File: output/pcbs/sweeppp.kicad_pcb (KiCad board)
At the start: 2 copper layers, 136.5 x 111 mm, 61 parts

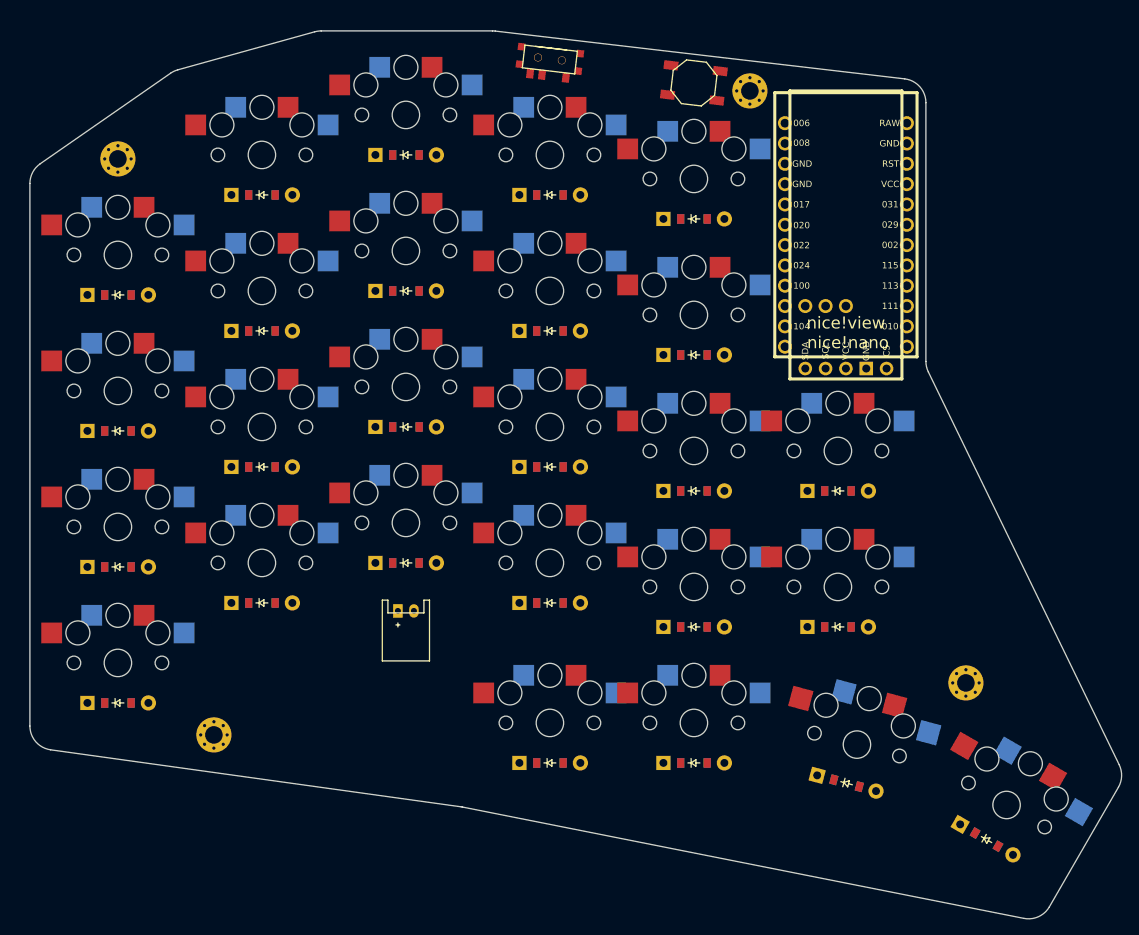
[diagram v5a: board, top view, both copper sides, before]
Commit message: Adjusted inner2 column to align with screen
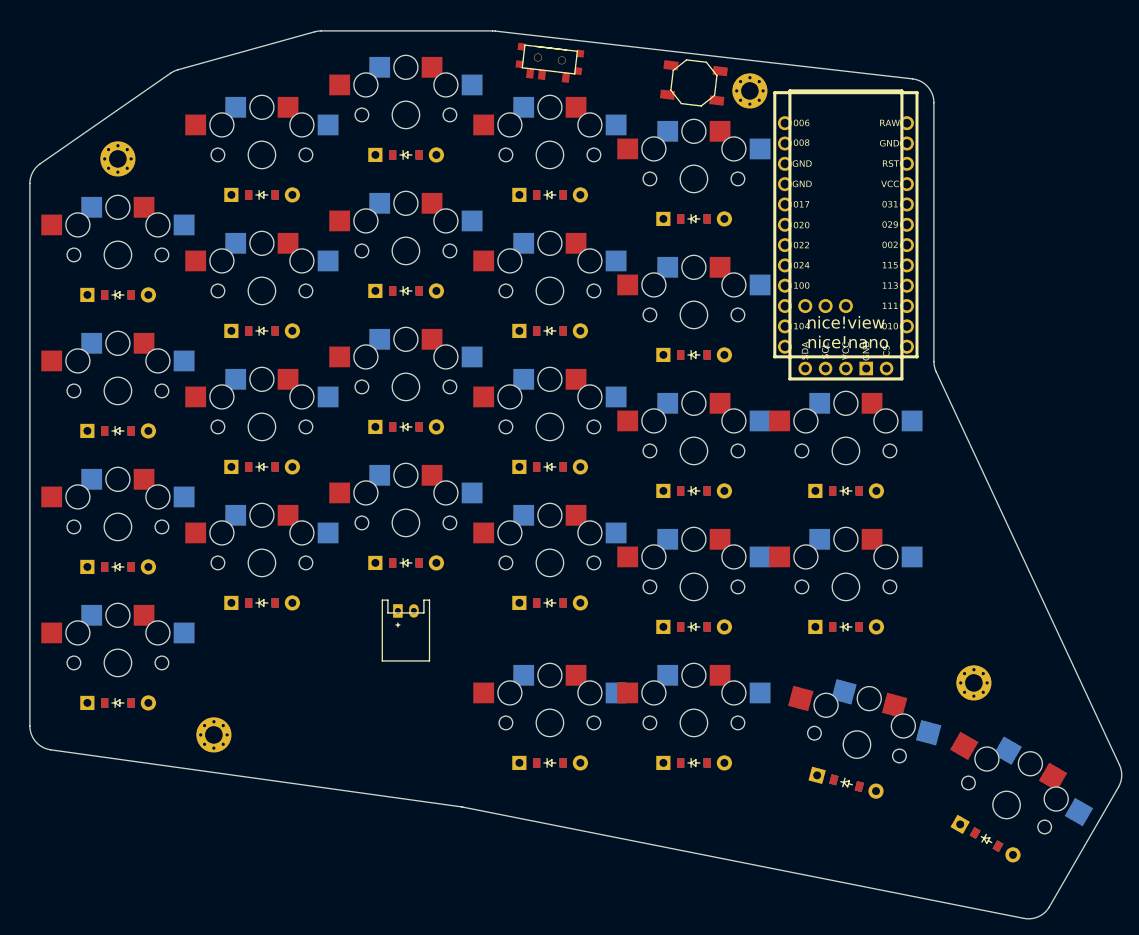
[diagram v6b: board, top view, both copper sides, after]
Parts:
- moved D21 1.00 mm to (191.0, 95.5)
- moved D22 1.00 mm to (191.0, 78.5)
- moved S21 1.00 mm to (191.0, 90.5)
- moved S22 1.00 mm to (191.0, 73.5)
- moved _4 1.00 mm to (207.0, 102.5)
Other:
- outline, holes or cut-outs redrawn
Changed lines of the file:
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@@
         )
       (module PG1350 (layer F.Cu)
-      (at 190 90.5 0)
+      (at 191 90.5 0)
       (fp_text reference "S21" (at 0 0) (layer F.SilkS) hide (effects (font (size 1.27 1.27) (thickness 0.15))))
       (fp_text value "" (at 0 0) (layer F.SilkS) hide (effects (font (size 1.27 1.27) (thickness 0.15))))
@@
         )
       (module PG1350 (layer F.Cu)
-      (at 190 73.5 0)
+      (at 191 73.5 0)
       (fp_text reference "S22" (at 0 0) (layer F.SilkS) hide (effects (font (size 1.27 1.27) (thickness 0.15))))
       (fp_text value "" (at 0 0) (layer F.SilkS) hide (effects (font (size 1.27 1.27) (thickness 0.15))))
@@
     )
     (module ComboDiode (layer F.Cu)
-        (at 190 95.5 0)
+        (at 191 95.5 0)
         (fp_text reference "D21" (at 0 0) (layer F.SilkS) hide (effects (font (size 1.27 1.27) (thickness 0.15))))
         (fp_text value "" (at 0 0) (layer F.SilkS) hide (effects (font (size 1.27 1.27) (thickness 0.15))))
@@
     )
     (module ComboDiode (layer F.Cu)
-        (at 190 78.5 0)
+        (at 191 78.5 0)
         (fp_text reference "D22" (at 0 0) (layer F.SilkS) hide (effects (font (size 1.27 1.27) (thickness 0.15))))
         (fp_text value "" (at 0 0) (layer F.SilkS) hide (effects (font (size 1.27 1.27) (thickness 0.15))))
@@
     )
     (module "MountingHole_2.2mm_M2_Pad_Via" (version 20210722) (generator pcbnew) (layer "F.Cu")
-      (at 206 102.5 0)
+      (at 207 102.5 0)
       (fp_text reference "_4" (at 0 -3.2) (layer "F.SilkS") hide
         (effects (font (size 1 1) (thickness 0.15)))
@@
 (gr_line (start 90.28881264685059 37.60499121746486) (end 106.58203879351727 26.29025083783523) (angle 90) (layer Edge.Cuts) (width 0.15))
 (gr_line (start 107.49029445382999 25.863807096158343) (end 124.60599322716334 21.109446325787964) (angle 90) (layer Edge.Cuts) (width 0.15))
-(gr_line (start 125.40892492 21) (end 146.8255916142857 21) (angle 90) (layer Edge.Cuts) (width 0.15))
-(gr_line (start 147.1732337257957 21.020210601342832) (end 198.34764211150997 26.990558246342825) (angle 90) (layer Edge.Cuts) (width 0.15))
-(gr_line (start 201 29.970347644999997) (end 201 62.30976752331668) (angle 90) (layer Edge.Cuts) (width 0.15))
-(gr_line (start 201.3016461 63.62083052331667) (end 225.1632542897898 112.73140977378557) (angle 90) (layer Edge.Cuts) (width 0.15))
-(gr_line (start 225.06297658978986 115.54247277378556) (end 216.43333215961238 130.48945531278997) (angle 90) (layer Edge.Cuts) (width 0.15))
+(gr_line (start 125.40892492 21) (end 146.82874165555558 21) (angle 90) (layer Edge.Cuts) (width 0.15))
+(gr_line (start 147.17014556686178 21.01948940129508) (end 199.34140391130617 26.995469902567795) (angle 90) (layer Edge.Cuts) (width 0.15))
+(gr_line (start 202 29.97598050127272) (end 202 62.334887266599594) (angle 90) (layer Edge.Cuts) (width 0.15))
+(gr_line (start 202.28109995616538 63.60279198704097) (end 225.19905252479415 112.74815065663205) (angle 90) (layer Edge.Cuts) (width 0.15))
+(gr_line (start 225.07822868095957 115.51605537707337) (end 216.43333215961243 130.48945531278986) (angle 90) (layer Edge.Cuts) (width 0.15))
 (gr_line (start 213.25166863674693 131.932145528087) (end 143.08502521190636 118.01686199984744) (angle 90) (layer Edge.Cuts) (width 0.15))
 (gr_line (start 142.91414307352233 117.9880754268781) (end 91.58729481551853 110.85934650215535) (angle 90) (layer Edge.Cuts) (width 0.15))
@@
 (gr_arc (start 108.29322614666665 28.75436077037037) (end 107.49029444666665 25.86380707037037) (angle -19.253716654027485) (layer Edge.Cuts) (width 0.15))
 (gr_arc (start 125.40892492 24) (end 125.40892492 21) (angle -15.524113143634992) (layer Edge.Cuts) (width 0.15))
-(gr_arc (start 146.8255916142857 24) (end 147.17323371428571 21.0202106) (angle -6.654425330555455) (layer Edge.Cuts) (width 0.15))
-(gr_arc (start 198 29.970347644999997) (end 201 29.970347644999997) (angle -83.34557466944511) (layer Edge.Cuts) (width 0.15))
-(gr_arc (start 204 62.30976752331668) (end 201 62.30976752331668) (angle -25.913963195184778) (layer Edge.Cuts) (width 0.15))
-(gr_arc (start 222.4649003897898 114.04247277378556) (end 225.0629765897898 115.54247277378556) (angle -55.9139633036003) (layer Edge.Cuts) (width 0.15))
-(gr_arc (start 213.8352559596124 128.98945531278997) (end 213.2516686596124 131.93214551278996) (angle -71.21721666545687) (layer Edge.Cuts) (width 0.15))
+(gr_arc (start 146.82874165555558 24) (end 147.17014555555556 21.0194894) (angle -6.534490900977929) (layer Edge.Cuts) (width 0.15))
+(gr_arc (start 199 29.97598050127272) (end 202 29.97598050127272) (angle -83.46550909902264) (layer Edge.Cuts) (width 0.15))
+(gr_arc (start 205 62.334887266599594) (end 202 62.334887266599594) (angle -25.001052542281315) (layer Edge.Cuts) (width 0.15))
+(gr_arc (start 222.48015248095953 114.01605537707343) (end 225.07822868095954 115.51605537707343) (angle -55.001052650696224) (layer Edge.Cuts) (width 0.15))
+(gr_arc (start 213.83525595961243 128.98945531278991) (end 213.25166865961242 131.9321455127899) (angle -71.21721666545847) (layer Edge.Cuts) (width 0.15))
 (gr_arc (start 142.5014378890409 120.95955221514457) (end 143.0850251890409 118.01686201514457) (angle -3.310052652139106) (layer Edge.Cuts) (width 0.15))
 (gr_arc (start 92 107.88786971388888) (end 89 107.88786971388888) (angle -82.09283587826559) (layer Edge.Cuts) (width 0.15))

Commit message: Routed pcb
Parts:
- MCU1: value nice_nano -> (none); footprint nice_nano -> ceoloide:mcu_nice_nano
- moved MCU1 3.25 mm to (189.3, 43.7), turned to 0 degrees
- moved T1 2.44 mm to (152.3, 22.7)
- moved S25 2.44 mm to (190.7, 108.4)
- moved D13 2.44 mm to (152.3, 90.7)
- moved niceView1 2.44 mm to (189.3, 62.7)
- moved S11 2.44 mm to (134.3, 46.7)
- moved _2 2.44 mm to (110.3, 107.2)
- moved D19 2.44 mm to (170.3, 59.7)
- moved D8 2.44 mm to (116.3, 39.7)
- moved _1 2.44 mm to (98.3, 35.2)
- moved D3 2.44 mm to (98.3, 69.2)
- moved D6 2.44 mm to (116.3, 73.7)
- moved S18 2.44 mm to (170.3, 71.7)
- moved S2 2.44 mm to (98.3, 81.2)
- moved S9 2.44 mm to (134.3, 80.7)
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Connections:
- net P006 renamed MCU1_1
- net P008 renamed MCU1_2
- net P029 renamed MCU1_19
- net P031 renamed MCU1_20
- D1 pad 1: P022 -> P7
- D10 pad 1: P024 -> P8
- D11 pad 1: P100 -> P16
- D12 pad 1: P011 -> P21
- D13 pad 1: P022 -> P7
- D14 pad 1: P024 -> P8
- D15 pad 1: P100 -> P16
- D16 pad 1: P011 -> P21
- D17 pad 1: P022 -> P7
- D18 pad 1: P024 -> P8
- D19 pad 1: P100 -> P16
- D2 pad 1: P024 -> P8
- D20 pad 1: P011 -> P21
- D21 pad 1: P022 -> P7
- D22 pad 1: P024 -> P8
- D23 pad 1: P104 -> P6
- D24 pad 1: P104 -> P6
- D25 pad 1: P104 -> P6
- D26 pad 1: P104 -> P6
- D3 pad 1: P100 -> P16
- D4 pad 1: P011 -> P21
- D5 pad 1: P022 -> P7
- D6 pad 1: P024 -> P8
- D7 pad 1: P100 -> P16
- D8 pad 1: P011 -> P21
- D9 pad 1: P022 -> P7
- MCU1 pad 10: P011 -> MCU1_10
- MCU1 pad 11: P104 -> MCU1_11
- MCU1 pad 12: P106 -> MCU1_12
- MCU1 pad 13: P009 -> MCU1_13
- MCU1 pad 14: P010 -> MCU1_14
- MCU1 pad 15: P111 -> MCU1_15
- MCU1 pad 16: P113 -> MCU1_16
- MCU1 pad 17: P115 -> MCU1_17
- MCU1 pad 18: P002 -> MCU1_18
- MCU1 pad 21: VCC -> MCU1_21
- MCU1 pad 22: RST -> MCU1_22
- MCU1 pad 23: GND -> MCU1_23
- MCU1 pad 24: RAW -> MCU1_24
- MCU1 pad 3: GND -> MCU1_3
- MCU1 pad 4: GND -> MCU1_4
- MCU1 pad 5: P017 -> MCU1_5
- MCU1 pad 6: P020 -> MCU1_6
- MCU1 pad 7: P022 -> MCU1_7
- MCU1 pad 8: P024 -> MCU1_8
- MCU1 pad 9: P100 -> MCU1_9
- S1 pad 1: P115 -> P20
- S10 pad 1: P111 -> P18
- S11 pad 1: P111 -> P18
- S12 pad 1: P111 -> P18
- S13 pad 1: P010 -> P15
- S14 pad 1: P010 -> P15
- S15 pad 1: P010 -> P15
- S16 pad 1: P010 -> P15
- S17 pad 1: P009 -> P10
- S18 pad 1: P009 -> P10
- S19 pad 1: P009 -> P10
- S2 pad 1: P115 -> P20
- S20 pad 1: P009 -> P10
- S21 pad 1: P106 -> P9
- S22 pad 1: P106 -> P9
- S23 pad 1: P111 -> P18
- S24 pad 1: P010 -> P15
- S25 pad 1: P009 -> P10
- S26 pad 1: P106 -> P9
- S3 pad 1: P115 -> P20
- S4 pad 1: P115 -> P20
- S5 pad 1: P113 -> P19
- S6 pad 1: P113 -> P19
- S7 pad 1: P113 -> P19
- S8 pad 1: P113 -> P19
- S9 pad 1: P111 -> P18
- niceView1 pad 1: P002 -> P4
- niceView1 pad 4: P020 -> P3
- niceView1 pad 5: P017 -> P2
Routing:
- net P20: track 0.00 -> 201.3 mm, vias 0 -> 4
- net P18: track 0.00 -> 192.4 mm, vias 0 -> 6
- net GND: track 0.00 -> 192.0 mm, vias 0 -> 1
- net P7: track 0.00 -> 179.3 mm
- net P19: track 0.00 -> 175.2 mm, vias 0 -> 4
- net P15: track 0.00 -> 172.4 mm, vias 0 -> 5
- net P8: track 0.00 -> 165.3 mm
- net P10: track 0.00 -> 157.9 mm, vias 0 -> 5
- net P6: track 0.00 -> 148.9 mm
- net P21: track 0.00 -> 129.4 mm
- net P16: track 0.00 -> 128.2 mm
- net P9: track 0.00 -> 109.2 mm, vias 0 -> 3
- net BAT: track 0.00 -> 77.7 mm, vias 0 -> 1
- net VCC: track 0.00 -> 47.8 mm
- net RAW: track 0.00 -> 45.2 mm
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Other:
- net class Default removed

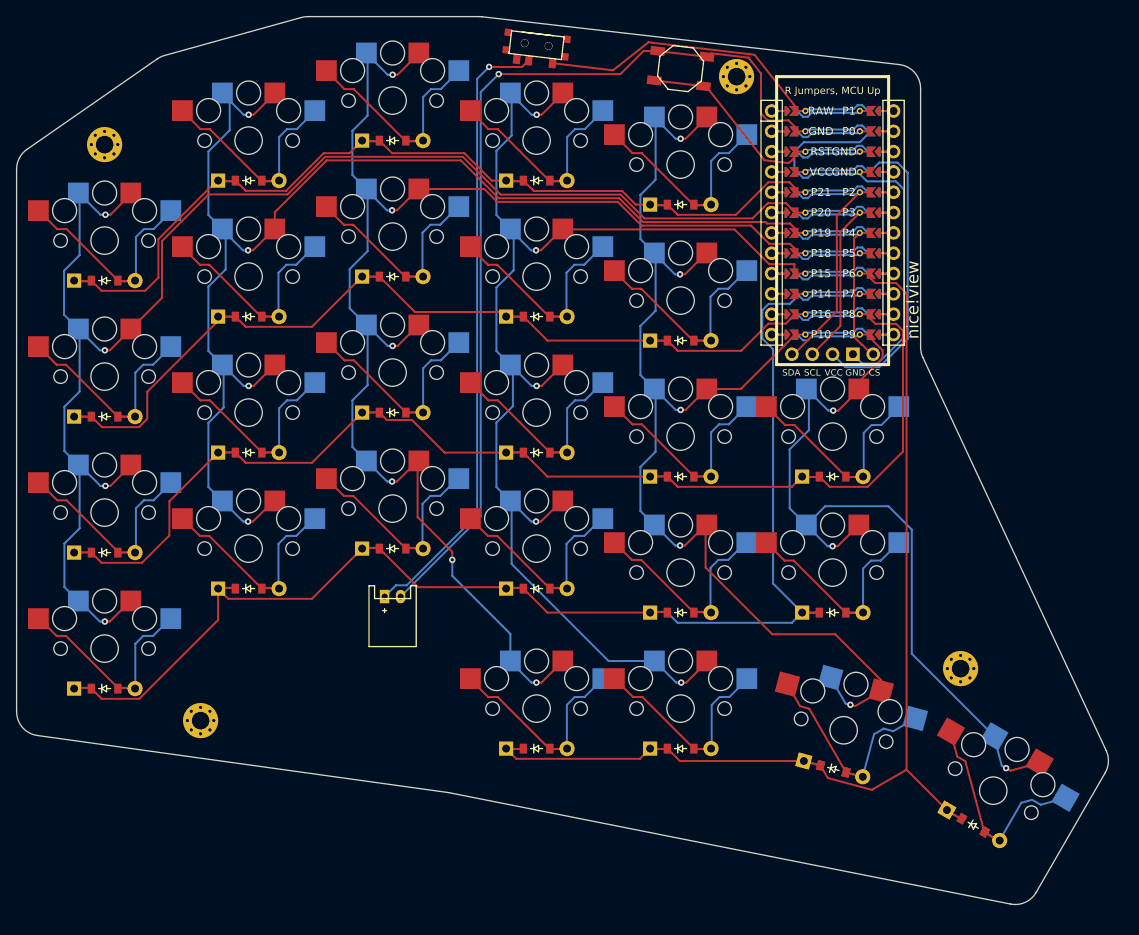
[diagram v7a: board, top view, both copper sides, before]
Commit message: switched to reversible nice!view
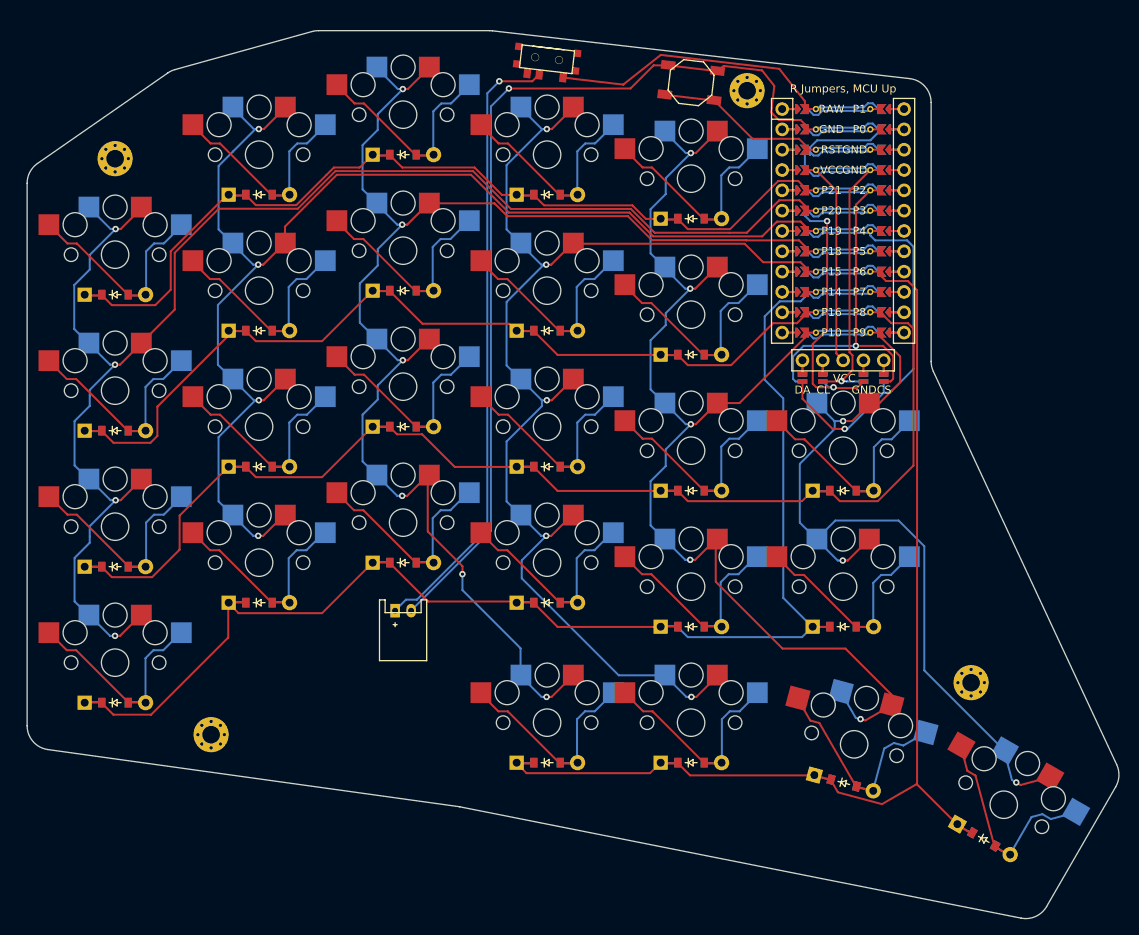
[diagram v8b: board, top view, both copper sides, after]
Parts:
- removed niceView1: niceView, lib:niceView_headers
- added DISP1: , ceoloide:display_nice_view, F.Cu at (190.7, 45.5)
- moved T1 2.20 mm to (153.7, 24.5)
- moved D13 2.20 mm to (153.7, 92.5)
- moved S25 2.20 mm to (192.0, 110.2)
- moved S11 2.20 mm to (135.7, 48.5)
- moved _2 2.20 mm to (111.7, 109.0)
- moved D19 2.20 mm to (171.7, 61.5)
- moved D8 2.20 mm to (117.7, 41.5)
- moved _1 2.20 mm to (99.7, 37.0)
- moved D3 2.20 mm to (99.7, 71.0)
- moved S2 2.20 mm to (99.7, 83.0)
- moved S18 2.20 mm to (171.7, 73.5)
- moved S9 2.20 mm to (135.7, 82.5)
- moved D17 2.20 mm to (171.7, 95.5)
- moved S5 2.20 mm to (117.7, 87.5)
- moved D2 2.20 mm to (99.7, 88.0)
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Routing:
- net P4: track 26.4 -> 53.8 mm, vias 0 -> 1
- net P2: track 33.7 -> 51.9 mm, vias 0 -> 1
- net P3: track 30.0 -> 43.1 mm, vias 0 -> 2
- net VCC: track 47.8 -> 35.0 mm
- net P15: track 172.4 -> 166.9 mm
- net P18: track 192.4 -> 187.9 mm
- net DISP1_5: track 0.00 -> 3.50 mm
- net DISP1_4: track 0.00 -> 3.50 mm
- net DISP1_2: track 0.00 -> 3.50 mm
- net DISP1_1: track 0.00 -> 3.50 mm
- net P7: track 179.3 -> 182.5 mm
- net P9: track 109.2 -> 112.0 mm
- net P10: track 157.9 -> 155.3 mm
- net P20: track 201.3 -> 198.9 mm
- net RST: track 32.9 -> 30.7 mm
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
